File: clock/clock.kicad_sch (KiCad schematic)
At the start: 19 parts, among them J1 Conn_01x06, J1 PJ-102AH, U1 ATmega328-PU, Y1 16MHz

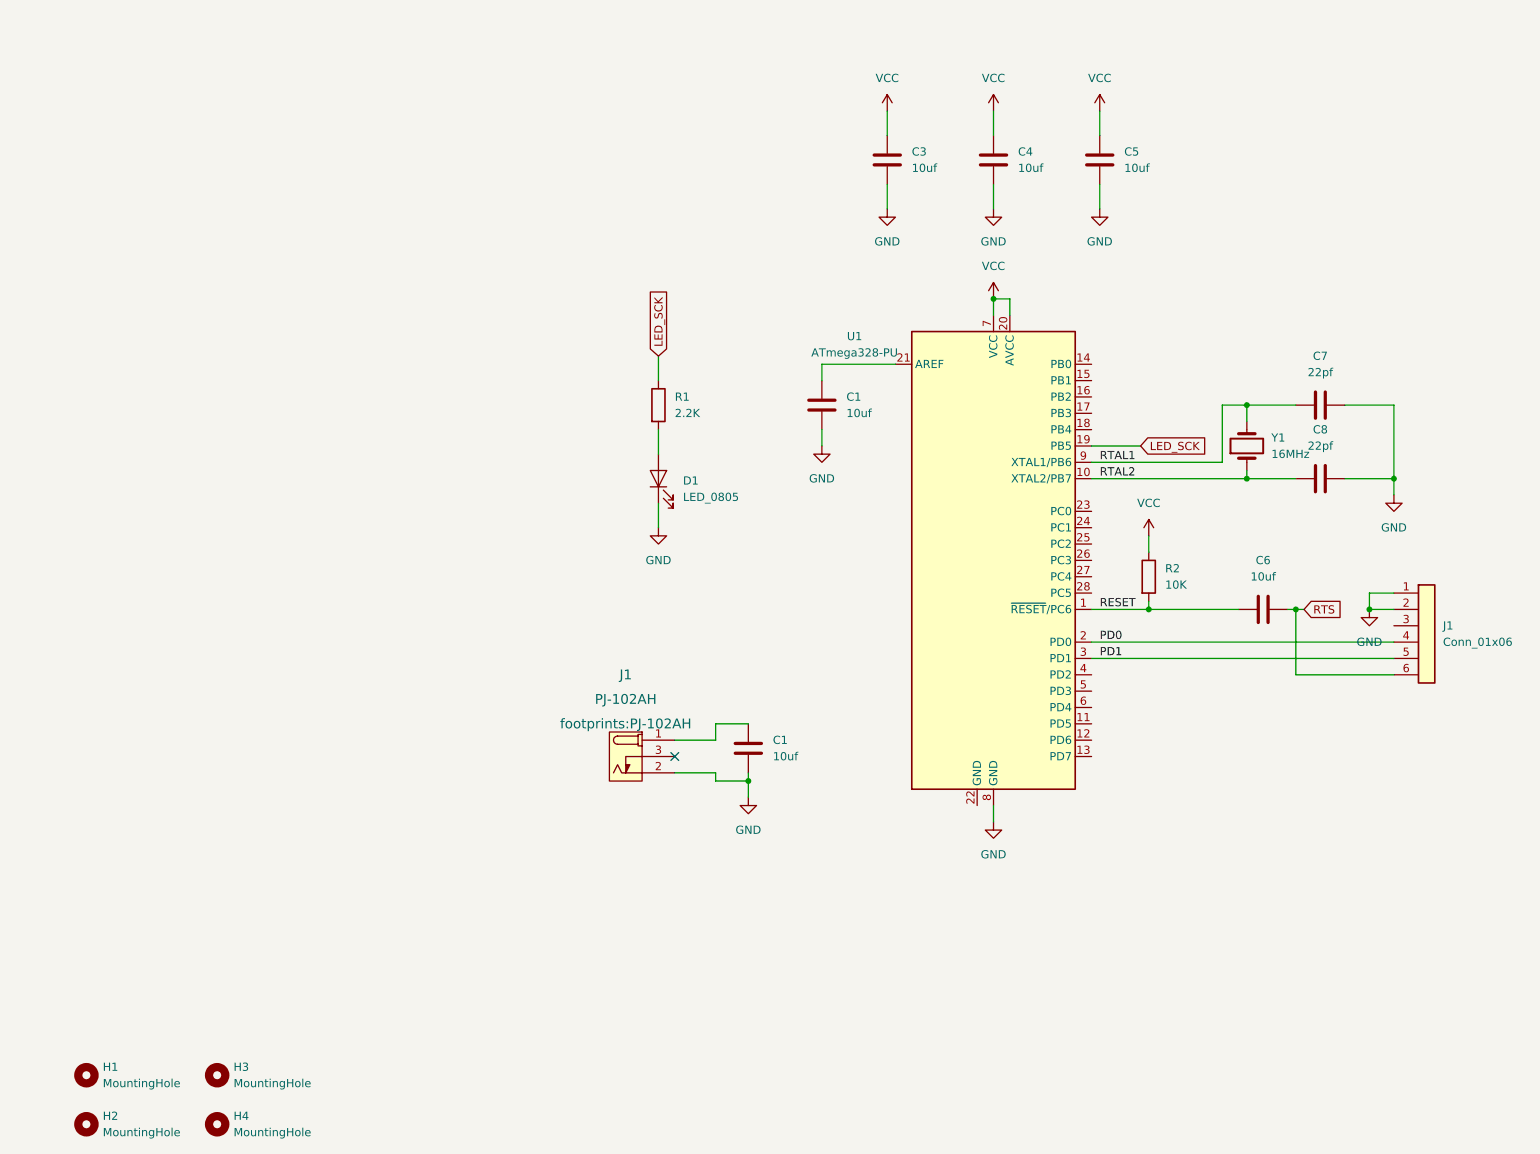
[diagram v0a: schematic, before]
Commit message: CPU, Crystal and power on schematic
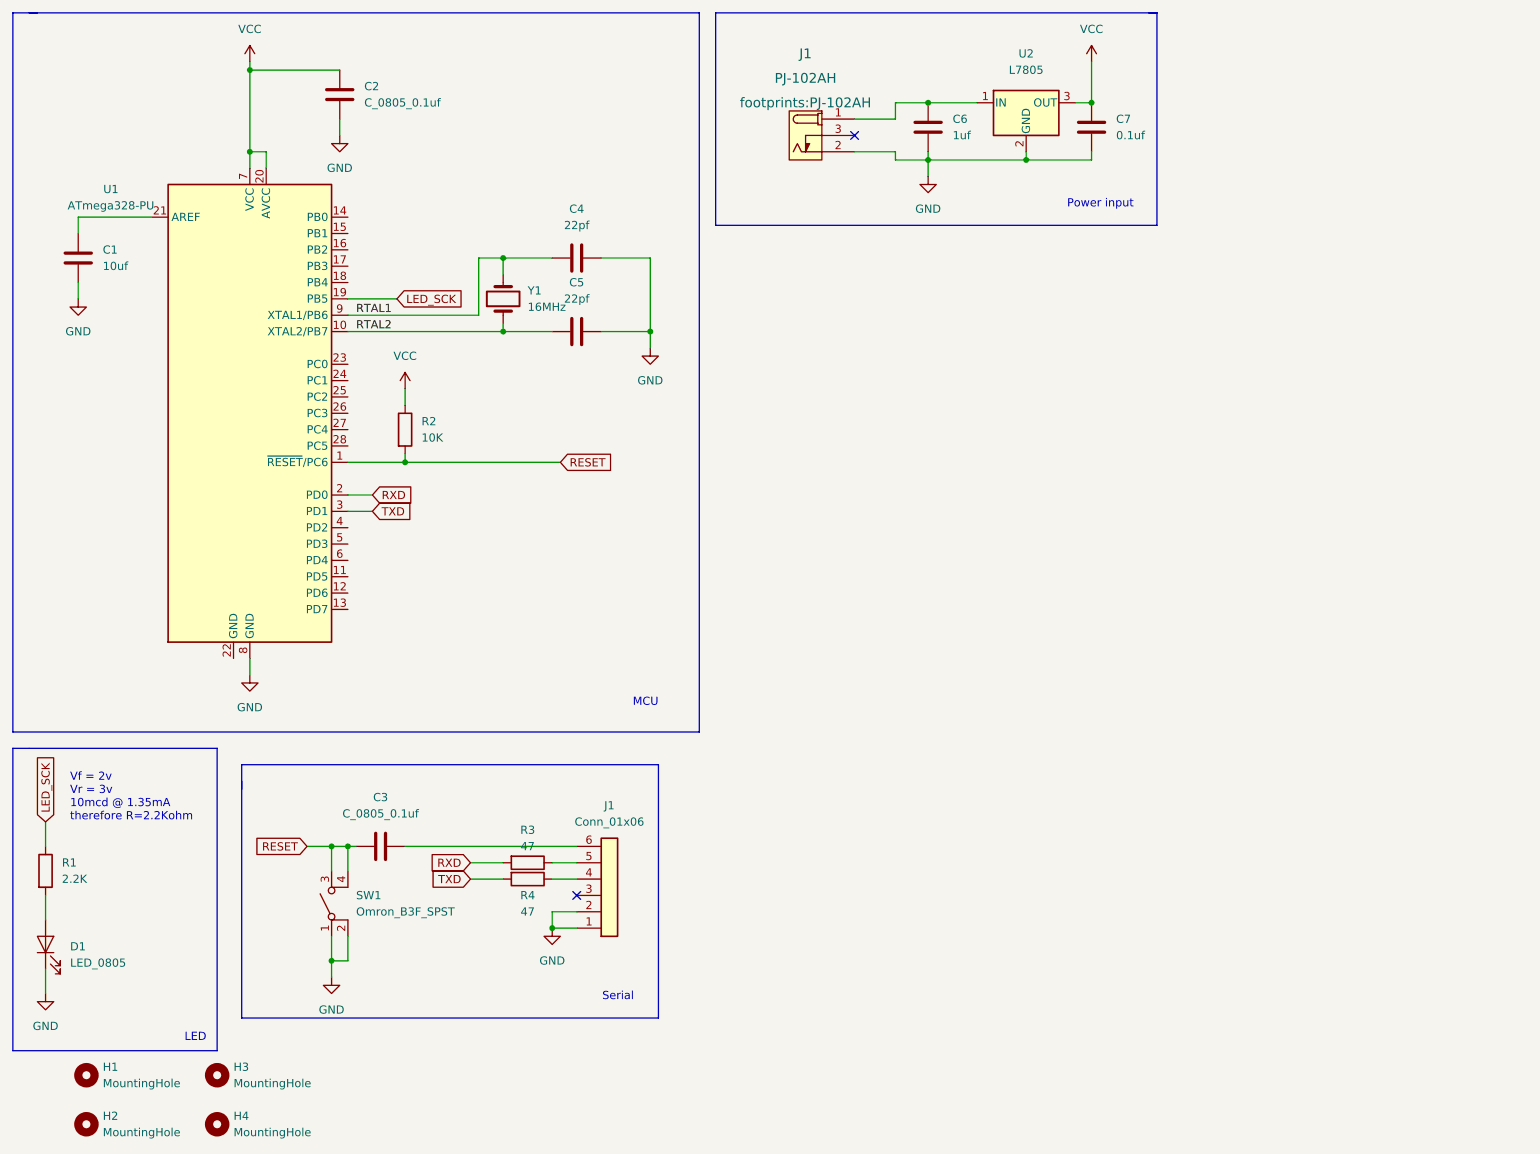
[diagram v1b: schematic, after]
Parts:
- removed C1, C3, C4, C5, C6: 10uf, footprints:C_0805_2012Metric, symbol HPS:C_0805_10uf
- added C2, C3: C_0805_0.1uf, footprints:C_0805_2012Metric, symbol HPS:C_0805_0.1uf
- added C6: 1uf, footprints:C_0805_2012Metric, symbol HPS:C_0805_1uf
- added C7: 0.1uf, footprints:C_0805_2012Metric, symbol HPS:C_0805_0.1uf
- added R3, R4: 47, footprints:R_0805_2012Metric, symbol HPS:R_0805_47
- added SW1: Omron_B3F_SPST, footprints:SW_SPST_Omron_B3FS-100xP, symbol HPS:Omron_B3F_SPST
- added U2: L7805, symbol HPS:L7805
- renumbered C7 to C4, C8 to C5
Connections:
- net GND: now also C2.2, C6.2, C7.2, SW1.1 (A), SW1.2 (A), U2.2 (GND)
- net RESET: now also C3.2, SW1.3 (B), SW1.4 (B)
- net VCC: now also C2.1, C7.1, U2.3 (OUT)
- net at J1.1 (POLE): now also C6.1, U2.1 (IN)
- net PD0: no longer names the net of J1.4 (Pin_4)
- net PD0: now also R4.1; no longer U1.2 (PD0)
- net PD1: no longer names the net of J1.5 (Pin_5)
- net PD1: now also R3.1; no longer U1.3 (PD1)
- net RTS: no longer names the net of J1.6 (Pin_6)
- net RTS: now also C3.1
- new net RXD: R3.2, U1.2 (PD0)
- new net TXD: R4.2, U1.3 (PD1)
- no-connect marks 1 -> 2
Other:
- note added: "LED"
- note added: "MCU"
- note added: "Power input"
- note added: "Serial"
- note added: "Vf = 2v Vr = 3v 10mcd @ 1.35mA therefore R=2.2Kohm"
- moved on the sheet: C1, C4, C5, D1, J1, R1, R2, U1, Y1

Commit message: update clock
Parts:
- added BT1: Battery_Cell, footprints:BatteryHolder_Keystone_106_1x20mm, symbol HPS:Battery_Cell
- added C8: C_0805_0.1uf, footprints:C_0805_2012Metric, symbol HPS:C_0805_0.1uf
- added C9: C_0805_10uf, footprints:C_0805_2012Metric, symbol HPS:C_0805_10uf
- added DS?: LED_Display_1001, footprints:Adafruit-1001-0-0-MFG, symbol HPS:LED_Display_1001
- added R10, R11, R12, R9: R_0805_10K, footprints:R_0805_2012Metric, symbol HPS:R_0805_10K
- added R?: R_0805_22K, footprints:R_0805_2012Metric, symbol HPS:R_0805_22K
- added SW1, SW2, SW3, SW4: Omron_B3F_SPST, footprints:SW_SPST_Omron_B3FS-100xP, symbol HPS:Omron_B3F_SPST
- added U3: MAX7219, footprints:DIP-24_W7.62mm, symbol HPS:MAX7219
- added U4: DS1307_DIP-8, footprints:DIP-8_W7.62mm, symbol HPS:DS1307_DIP-8
- added Y2: Crystal_32768Hz, footprints:Crystal_SMD_2Pin_3.2x1.5mm, symbol HPS:Crystal_32768Hz
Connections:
- net GND: now also BT1.2 (-), C8.2, C9.2, SW1.1 (A), SW1.2 (A), SW2.1 (A), SW2.2 (A), SW3.1 (A), SW3.2 (A), SW4.1 (A), SW4.2 (A), U3.4 (GND), U3.9 (GND), U4.4 (GND)
- net VCC: now also C8.1, C9.1, R10.1, R11.1, R12.1, R9.1, R?.1, U3.19 (V+), U4.8 (VCC)
- new net: R?.2, U3.18 (ISET)
- new net BTN_ALARM: R9.2, SW1.3 (B), SW1.4 (B)
- new net BTN_DWN: R10.2, SW2.3 (B), SW2.4 (B)
- new net BTN_PAUSE: R12.2, SW4.3 (B), SW4.4 (B)
- new net BTN_UP: R11.2, SW3.3 (B), SW3.4 (B)
- new net DIG_0: DS?.14 (COM_DIG.1), U3.2 (DIG_0)
- new net DIG_1: DS?.11 (COM_DIG.2), U3.11 (DIG_1)
- new net DIG_2: DS?.10 (COM_DIG.3), U3.6 (DIG_2)
- new net DIG_3: DS?.6 (COM_DIG.4), U3.7 (DIG_3)
- new net DIG_4: DS?.7 (COM_COLON), U3.3 (DIG_4)
- new net DISP_CLK: U3.13 (CLK)
- new net DISP_DATA: U3.1 (DIN)
- new net DISP_LOAD: U3.12 (LOAD)
- new net RTC_XTAL1: U4.1 (X1), Y2.1
- new net RTC_XTAL2: U4.2 (X2), Y2.2
- new net SCL: U4.6 (SCL)
- new net SDA: U4.5 (SDA)
- new net SEG_A: DS?.13 (A), U3.14 (SEG_A)
- new net SEG_B: DS?.9 (B), U3.16 (SEG_B)
- new net SEG_C: DS?.4 (C), U3.20 (SEG_C)
- new net SEG_D: DS?.2 (D), U3.23 (SEG_D)
- new net SEG_DP: DS?.3 (DP), DS?.8 (COLON), U3.22 (SEG_DP)
- new net SEG_E: DS?.1 (E), U3.21 (SEG_E)
- new net SEG_F: DS?.12 (F), U3.15 (SEG_F)
- new net SEG_G: DS?.5 (G), U3.17 (SEG_G)
- new net VBAT: BT1.1 (+), U4.3 (VBAT)
- no-connect marks 2 -> 7
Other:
- note added: "Buttons"
- note added: "Display"
- note added: "Mechanical"
- note added: "Real time clock"
- moved on the sheet: C3, C6, C7, D1, H1, H2, H3, H4, J1, R1, R3, R4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

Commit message: updated clock
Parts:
- added BZ1: Buzzer, footprints:Buzzer_TDK_PS1240P02BT_D12.2mm_H6.5mm, symbol HPS:Buzzer
- added C10, C11, C12, C13, C14, C15, C16, C17, C18, C19, C20, C21, C22, C23, C24, C25, C26, C27, C28, C29, C30, C31, C32, C33, C34, C35, C36, C37, C38, C39, C40, C41, C42, C43, C44, C45, C46, C47, C48, C49: 0.1uf, footprints:C_0805_2012Metric, symbol HPS:0.1uf
- added D1, D10, D11, D12, D13, D14, D15, D16, D17, D18, D19, D2, D20, D21, D22, D23, D24, D25, D26, D27, D28, D29, D3, D30, D31, D32, D33, D34, D35, D36, D37, D38, D39, D4, D40, D5, D6, D7, D8, D9: NEOPIXEL_SMT, footprints:LED_SK6812_PLCC4_5.0x5.0mm_P3.2mm, symbol HPS:NEOPIXEL_SMT
- added J3: Conn_02x03_Odd_Even, footprints:PinHeader_2x03_P2.54mm_Vertical, symbol HPS:Conn_02x03_Odd_Even
- added R13: R_0805_47, footprints:R_0805_2012Metric, symbol HPS:R_0805_47
- added R14, R15: 4.7K, footprints:R_0805_2012Metric, symbol HPS:R_0805_4.7K
- gave numbers to parts that had none: 2
- renumbered D1 to D50, J1 to J2, SW1 to SW5
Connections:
- net BTN_ALARM: now also U1.6 (PD4)
- net BTN_DWN: now also U1.5 (PD3)
- net BTN_PAUSE: now also U1.11 (PD5)
- net BTN_UP: now also U1.4 (PD2)
- net DISP_CLK: now also U1.15 (PB1)
- net DISP_DATA: now also U1.16 (PB2)
- net DISP_LOAD: now also U1.14 (PB0)
- net GND: now also BZ1.2 (+), D1.1 (VSS), D10.1 (VSS), D11.1 (VSS), D12.1 (VSS), D13.1 (VSS), D14.1 (VSS), D15.1 (VSS), D16.1 (VSS), D17.1 (VSS), D18.1 (VSS), D19.1 (VSS), D2.1 (VSS), D20.1 (VSS), D21.1 (VSS), D22.1 (VSS), D23.1 (VSS), D24.1 (VSS), D25.1 (VSS), D26.1 (VSS), D27.1 (VSS), D28.1 (VSS), D29.1 (VSS), D3.1 (VSS), D30.1 (VSS), D31.1 (VSS), D32.1 (VSS), D33.1 (VSS), D34.1 (VSS), D35.1 (VSS), D36.1 (VSS), D37.1 (VSS), D38.1 (VSS), D39.1 (VSS), D4.1 (VSS), D40.1 (VSS), D5.1 (VSS), D6.1 (VSS), D7.1 (VSS), D8.1 (VSS), D9.1 (VSS), J3.6 (Pin_6)
- net LED_SCK: now also J3.3 (Pin_3)
- net RESET: now also J3.5 (Pin_5)
- net SCL: now also U1.28 (PC5), R14.2
- net SDA: now also U1.27 (PC4), R15.2
- net VCC: now also C10.2, C11.2, C12.2, C13.2, C14.2, C15.2, C16.2, C17.2, C18.2, C19.2, C20.2, C21.2, C22.2, C23.2, C24.2, C25.2, C26.2, C27.2, C28.2, C29.2, C30.2, C31.2, C32.2, C33.2, C34.2, C35.2, C36.2, C37.2, C38.2, C39.2, C40.2, C41.2, C42.2, C43.2, C44.2, C45.2, C46.2, C47.2, C48.2, C49.2, J3.2 (Pin_2), R14.1, R15.1
- net NEO: now reaches U1.12 (PD6)
- net NEO: now also U3.10 (DIG_5), D1.2 (DIN)
- net BUZZER: now reaches U1.13 (PD7)
- net BUZZER: now also R13.2
- new net: C48.1, D32.3 (VDD)
- new net: C11.1, D2.3 (VDD)
- new net: D37.2 (DIN), D38.4 (DOUT)
- new net: C43.1, D37.3 (VDD)
- new net: D36.2 (DIN), D37.4 (DOUT)
- new net: D38.2 (DIN), D39.4 (DOUT)
- new net: C42.1, D38.3 (VDD)
- new net: C22.1, D18.3 (VDD)
- new net: D32.2 (DIN), D33.4 (DOUT)
- new net: D31.2 (DIN), D32.4 (DOUT)
- new net: C21.1, D19.3 (VDD)
- new net: D5.4 (DOUT), D6.2 (DIN)
- new net: C15.1, D6.3 (VDD)
- new net: D6.4 (DOUT), D7.2 (DIN)
- new net: C49.1, D31.3 (VDD)
- new net: C13.1, D4.3 (VDD)
- new net: C34.1, D25.3 (VDD)
- new net: C44.1, D36.3 (VDD)
- new net: D35.2 (DIN), D36.4 (DOUT)
- new net: D27.4 (DOUT), D28.2 (DIN)
- new net: C37.1, D28.3 (VDD)
- new net: D28.4 (DOUT), D29.2 (DIN)
- new net: C46.1, D34.3 (VDD)
- new net: C16.1, D7.3 (VDD)
- new net: D7.4 (DOUT), D8.2 (DIN)
- new net: D19.2 (DIN), D20.4 (DOUT)
- new net: D18.2 (DIN), D19.4 (DOUT)
- new net: BZ1.1 (-), R13.1
- new net: C38.1, D29.3 (VDD)
- new net: C39.1, D30.3 (VDD)
- new net: D17.2 (DIN), D18.4 (DOUT)
- new net: C23.1, D17.3 (VDD)
- new net: D16.2 (DIN), D17.4 (DOUT)
- new net: D29.4 (DOUT), D30.2 (DIN)
- new net: D30.4 (DOUT), D40.2 (DIN)
- new net: D23.4 (DOUT), D24.2 (DIN)
- new net: C33.1, D24.3 (VDD)
- new net: D24.4 (DOUT), D25.2 (DIN)
- new net: D25.4 (DOUT), D26.2 (DIN)
- new net: D1.4 (DOUT), D2.2 (DIN)
- new net: D2.4 (DOUT), D3.2 (DIN)
- new net: D22.4 (DOUT), D23.2 (DIN)
- new net: C32.1, D23.3 (VDD)
- new net: D39.2 (DIN), D40.4 (DOUT)
- new net: C41.1, D39.3 (VDD)
- new net: C20.1, D20.3 (VDD)
- new net: D13.2 (DIN), D14.4 (DOUT)
- new net: C27.1, D13.3 (VDD)
- new net: D12.2 (DIN), D13.4 (DOUT)
- new net: C26.1, D14.3 (VDD)
- new net: D21.4 (DOUT), D22.2 (DIN)
- new net: C31.1, D22.3 (VDD)
- new net: D11.4 (DOUT), D21.2 (DIN)
- new net: C30.1, D21.3 (VDD)
- new net: D34.2 (DIN), D35.4 (DOUT)
- new net: D33.2 (DIN), D34.4 (DOUT)
- new net: C28.1, D12.3 (VDD)
- new net: D11.2 (DIN), D12.4 (DOUT)
- new net: D8.4 (DOUT), D9.2 (DIN)
- new net: C18.1, D9.3 (VDD)
- new net: D10.2 (DIN), D9.4 (DOUT)
- new net: C17.1, D8.3 (VDD)
- new net: C29.1, D11.3 (VDD)
- new net: D26.4 (DOUT), D27.2 (DIN)
- new net: C36.1, D27.3 (VDD)
- new net: D4.4 (DOUT), D5.2 (DIN)
- new net: C14.1, D5.3 (VDD)
- new net: C19.1, D10.3 (VDD)
- new net: C24.1, D16.3 (VDD)
- new net: D15.2 (DIN), D16.4 (DOUT)
- new net: C35.1, D26.3 (VDD)
- new net: C25.1, D15.3 (VDD)
- new net: D14.2 (DIN), D15.4 (DOUT)
- new net: D10.4 (DOUT), D20.2 (DIN)
- new net: C12.1, D3.3 (VDD)
- new net: D3.4 (DOUT), D4.2 (DIN)
- new net: C40.1, D40.3 (VDD)
- new net: C47.1, D33.3 (VDD)
- new net: C10.1, D1.3 (VDD)
- new net: C45.1, D35.3 (VDD)
- new net MISO: J3.1 (Pin_1)
- new net MOSI: J3.4 (Pin_4)
- no-connect marks 7 -> 6
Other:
- note added: "BUTTONS"
- note added: "BUZZER"
- note added: "DISPLAY"
- note added: "ISCP"
- note added: "MECHANICAL"
- note added: "NEO-PIXELS"
- note added: "POWER INPUT"
- note added: "REAL TIME CLOCK"
- note added: "SERIAL"
- note removed: "Buttons"
- note removed: "Display"
- note removed: "Mechanical"
- note removed: "Power input"
- note removed: "Real time clock"
- note removed: "Serial"
- moved on the sheet: BT1, C3, C6, C7, C8, C9, D50, DS1, H1, H2, H3, H4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

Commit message: update
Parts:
- removed C10, C11, C12, C13, C14, C15, C16, C17, C18, C19, C20, C21, C22, C23, C24, C25, C26, C27, C28, C29, C30, C31, C32, C33, C34, C35, C36, C37, C38, C39, C40, C41, C42, C43, C44, C45, C46, C47, C48, C49: 0.1uf, footprints:C_0805_2012Metric, symbol HPS:0.1uf
- added C10, C11, C12, C13: 10uf, footprints:C_0805_2012Metric, symbol HPS:C_0805_10uf
- added U5: UltrasonicModule, footprints:HC-SR04_Horiz, symbol HPS:UltrasonicModule
- U2: footprint (none) -> footprints:TO-252-2
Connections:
- net BTN_DWN: now also U1.13 (PD7); no longer U1.5 (PD3)
- net BUZZER: now also U1.5 (PD3); no longer U1.13 (PD7)
- net GND: now also C10.2, C11.2, C12.2, C13.2, U5.4 (GND)
- net MISO: now also U1.18 (PB4)
- net MOSI: now also U1.17 (PB3)
- net NEO: no longer U3.10 (DIG_5)
- net VCC: now also D1.3 (VDD), D10.3 (VDD), D11.3 (VDD), D12.3 (VDD), D13.3 (VDD), D14.3 (VDD), D15.3 (VDD), D16.3 (VDD), D17.3 (VDD), D18.3 (VDD), D19.3 (VDD), D2.3 (VDD), D20.3 (VDD), D21.3 (VDD), D22.3 (VDD), D23.3 (VDD), D24.3 (VDD), D25.3 (VDD), D26.3 (VDD), D27.3 (VDD), D28.3 (VDD), D29.3 (VDD), D3.3 (VDD), D30.3 (VDD), D31.3 (VDD), D32.3 (VDD), D33.3 (VDD), D34.3 (VDD), D35.3 (VDD), D36.3 (VDD), D37.3 (VDD), D38.3 (VDD), D39.3 (VDD), D4.3 (VDD), D40.3 (VDD), D5.3 (VDD), D6.3 (VDD), D7.3 (VDD), D8.3 (VDD), D9.3 (VDD), C10.1, C11.1, C12.1, C13.1, U5.1 (VCC)
- net at D38.4 (DOUT): now also D39.2 (DIN); no longer D37.2 (DIN)
- net at D36.2 (DIN): now also D35.4 (DOUT); no longer D37.4 (DOUT)
- net at D39.4 (DOUT): now also D40.2 (DIN); no longer D38.2 (DIN)
- net at D32.2 (DIN): now also D31.4 (DOUT); no longer D33.4 (DOUT)
- net at D31.2 (DIN): now also D30.4 (DOUT); no longer D32.4 (DOUT)
- net at D35.2 (DIN): now also D34.4 (DOUT); no longer D36.4 (DOUT)
- net at D19.2 (DIN): now also D18.4 (DOUT); no longer D20.4 (DOUT)
- net at D19.4 (DOUT): now also D20.2 (DIN); no longer D18.2 (DIN)
- net at D17.2 (DIN): now also D16.4 (DOUT); no longer D18.4 (DOUT)
- net at D16.2 (DIN): now also D15.4 (DOUT); no longer D17.4 (DOUT)
- net at D40.4 (DOUT): no longer D39.2 (DIN)
- net at D14.4 (DOUT): now also D15.2 (DIN); no longer D13.2 (DIN)
- net at D13.4 (DOUT): now also D14.2 (DIN); no longer D12.2 (DIN)
- net at D21.2 (DIN): now also D20.4 (DOUT); no longer D11.4 (DOUT)
- net at D34.2 (DIN): now also D33.4 (DOUT); no longer D35.4 (DOUT)
- net at D33.2 (DIN): now also D32.4 (DOUT); no longer D34.4 (DOUT)
- net at D12.4 (DOUT): now also D13.2 (DIN); no longer D11.2 (DIN)
- net at D10.4 (DOUT): now also D11.2 (DIN); no longer D20.2 (DIN)
- net TRIG: now reaches U1.23 (PC0)
- net TRIG: now also U5.2 (TRIG)
- net ECHO: now reaches U1.24 (PC1)
- net ECHO: now also U5.3 (ECHO)
- new net: D11.4 (DOUT), D12.2 (DIN)
- new net: D17.4 (DOUT), D18.2 (DIN)
- new net: D37.4 (DOUT), D38.2 (DIN)
- new net: D36.4 (DOUT), D37.2 (DIN)
- no-connect marks 6 -> 7
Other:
- note added: "NEO Capacitors"
- note added: "ultrasonic Sensor"
- moved on the sheet: BZ1, C3, C6, C7, D1, D10, D2, D3, D4, D5, D50, D6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

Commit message: pcb-changes
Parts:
- removed C7: 0.1uf, footprints:C_0805_2012Metric, symbol HPS:C_0805_0.1uf
- added C7: C_0805_1uf, footprints:C_0805_2012Metric, symbol HPS:C_0805_1uf
- C2, C3, C8: symbol HPS:C_0805_0.1uf -> HPS:C_0805_1uf; Digikey PN 478-1395-1-ND -> 311-1456-1-ND; MFG AVX Corporation -> Yageo; MPN 08055C104KAT2A -> CC0805KKX7R8BB105
- U2: Digikey PN (none) -> 497-7255-1-ND; MFG (none) -> STMicroelectronics; MPN (none) -> L7805CDT-TR
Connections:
- net GND: now also U1.22 (GND), C7.2
- net VCC: now also C7.1; no longer D10.3 (VDD)

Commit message: pcb
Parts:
- removed J1: PJ-102AH, footprints:PJ-102AH, symbol HPS:PJ-102AH
- added J1: Power_inlet_vertical, footprints:Wurth-694106402002, symbol HPS:Power_inlet_vertical
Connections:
- net GND: now also J1.2 (OUT)
- net at C6.1, U2.1 (IN): now also J1.1 (POLE)
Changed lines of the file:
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@@
     (pin "1")
   )
-  (symbol (lib_id "HPS:PJ-102AH") (at 156.21 148.59 0) (unit 1)
-    (in_bom yes) (on_board yes) (fields_autoplaced)
-    (property "Reference" "J1" (id 0) (at 153.67 135.89 0)
-      (effects (font (size 1.524 1.524)))
-    )
-    (property "Value" "PJ-102AH" (id 1) (at 153.67 139.7 0)
-      (effects (font (size 1.524 1.524)))
-    )
-    (property "Footprint" "footprints:PJ-102AH" (id 2) (at 153.67 143.51 0)
-      (effects (font (size 1.524 1.524)))
-    )
-    (property "Datasheet" "https://www.cuidevices.com/product/resource/pj-102ah.pdf" (id 3) (at 157.734 160.528 0)
-      (effects (font (size 1.524 1.524)) hide)
-    )
-    (property "MFG" "CUI Devices" (id 4) (at 156.21 166.37 0)
-      (effects (font (size 1.27 1.27)) hide)
-    )
-    (property "MPN" "PJ-102AH" (id 5) (at 156.21 168.91 0)
-      (effects (font (size 1.27 1.27)) hide)
-    )
-    (property "Digikey PN" "CP-102AH-ND" (id 6) (at 157.734 174.117 0)
-      (effects (font (size 1.27 1.27)) hide)
-    )
-    (property "Mouser PN" "490-PJ-102AH" (id 7) (at 156.21 171.323 0)
-      (effects (font (size 1.27 1.27)) hide)
-    )
-    (pin "1")
-    (pin "2")
-    (pin "3")
-  )
   (symbol (lib_id "HPS:DS1307_DIP-8") (at 186.69 44.45 0) (unit 1)
     (in_bom yes) (on_board yes) (fields_autoplaced)
@@
     (pin "4")
   )
+  (symbol (lib_id "HPS:Power_inlet_vertical") (at 156.21 148.59 0) (unit 1)
+    (in_bom yes) (on_board yes)
+    (property "Reference" "J1" (id 0) (at 153.67 135.89 0)
+      (effects (font (size 1.524 1.524)))
+    )
+    (property "Value" "Power_inlet_vertical" (id 1) (at 153.67 139.7 0)
+      (effects (font (size 1.524 1.524)))
+    )
+    (property "Footprint" "footprints:Wurth-694106402002" (id 2) (at 160.02 154.94 0)
+      (effects (font (size 1.524 1.524)))
+    )
+    (property "Datasheet" "https://www.we-online.com/katalog/datasheet/6941xx402002.pdf" (id 3) (at 157.734 160.528 0)
+      (effects (font (size 1.524 1.524)) hide)
+    )
+    (property "MFG" "Wurth" (id 4) (at 156.21 166.37 0)
+      (effects (font (size 1.27 1.27)) hide)
+    )
+    (property "MPN" "694106402002" (id 5) (at 156.21 168.91 0)
+      (effects (font (size 1.27 1.27)) hide)
+    )
+    (property "Digikey PN" "732-5931-ND" (id 6) (at 157.734 174.117 0)
+      (effects (font (size 1.27 1.27)) hide)
+    )
+    (pin "1")
+    (pin "2")
+    (pin "3")
+  )
   (symbol (lib_id "HPS:GND") (at 363.22 193.04 0) (unit 1)
     (in_bom yes) (on_board yes) (fields_autoplaced)
@@
   (symbol (lib_id "HPS:GND") (at 48.26 118.11 0) (unit 1)
     (in_bom yes) (on_board yes)
-    (property "Reference" "#PWR?" (id 0) (at 48.26 124.46 0)
+    (property "Reference" "#PWR0222" (id 0) (at 48.26 124.46 0)
       (effects (font (size 1.27 1.27)) hide)
     )
@@
     )
     (path "/d59759b3-e7f2-42b5-b064-e6d49d7e3fb8"
-      (reference "#PWR?") (unit 1) (value "GND") (footprint "")
+      (reference "#PWR0222") (unit 1) (value "GND") (footprint "")
     )
     (path "/38df633d-09e2-463b-8e37-6093e12f6b9e"
@@
       (reference "H4") (unit 1) (value "MountingHole") (footprint "footprints:MountingHole_3.2mm_M3")
     )
-    (path "/53154f9f-55da-4a17-a5d4-ab5962bddb30"
-      (reference "J1") (unit 1) (value "PJ-102AH") (footprint "footprints:PJ-102AH")
+    (path "/a1681212-73ed-437a-9825-3188d7ac9e81"
+      (reference "J1") (unit 1) (value "Power_inlet_vertical") (footprint "footprints:Wurth-694106402002")
     )
     (path "/15b638ed-17ab-4c83-b0db-6b4905599093"
